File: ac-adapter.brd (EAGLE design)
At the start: 98.4 x 49.5 mm, 55 parts, among them IC1 STR-Y6735, IC2 TL431, Q1 TLP621-1, T1 COMMON_FILTER-SU10VFC, T2 TRANSFORMAER_FLYBACK-PQ2620

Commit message: 微修正
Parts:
- added HT1: HEATSINK-2, my_connector:HEATSINK2
- D5, D6: value 0.1A -> 1N4148; device my_rcl:D0207/2V -> my_rcl:SOD123
- R3: device my_rcl:0207/2V -> my_rcl:1608
- R7, R8: device my_rcl:0207/2V -> my_rcl:2012
- moved C5 2.69 mm to (14.6, 8.26)
- moved IC1 2.29 mm to (26.7, 8.26)
- moved D5 2.25 mm to (23.5, 18.1), flipped to the bottom
- moved D6 2.06 mm to (26.7, 16.7), flipped to the bottom, turned to 0 degrees
- moved C3 1.91 mm to (35.6, 16.5)
- moved R3 1.91 mm to (26.7, 19.1), flipped to the bottom, turned to 180 degrees
- moved R4 1.91 mm to (21.3, 18.1)
- moved C4 1.90 mm to (35.6, 13.0)
- moved C6 1.90 mm to (21.3, 14.3)
- moved C7 1.90 mm to (24.1, 6.35)
- moved R5 1.90 mm to (19.4, 14.3)
- moved R1 1.90 mm to (30.2, 21.9)
- moved C17 1.27 mm to (29.8, 23.2)
- moved SJ1 0.79 mm to (84.0, 6.67)
- moved R7 0.71 mm to (80.6, 11.7), flipped to the bottom
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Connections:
- net PGND: now also HT1.HT1
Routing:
- net PGND: track 138.9 -> 151.5 mm
- net VCC: track 22.0 -> 28.7 mm
- net SW: track 33.3 -> 31.4 mm
- net N$15: track 38.3 -> 36.7 mm
- net N$6: track 29.2 -> 30.6 mm
- net N$11: track 13.3 -> 12.2 mm
- net V+: track 31.5 -> 32.4 mm
- net N$23: track 27.4 -> 26.7 mm
- net VP: track 26.5 -> 25.9 mm
- net N$10: track 4.49 -> 5.13 mm
- removed copper zone on layer 1, net PGND
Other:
- board text added: "QR AC adapter"
- board text removed: "QR AC adapter ±20V2A"

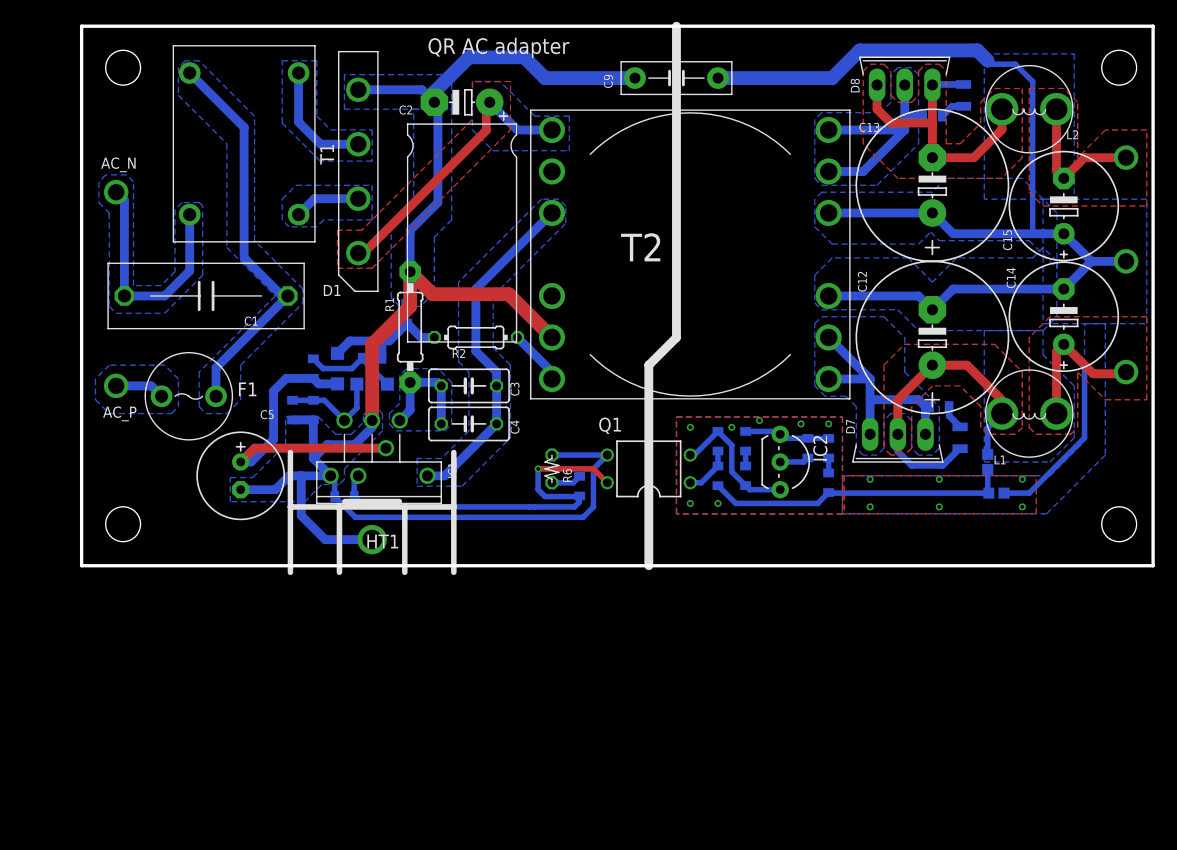
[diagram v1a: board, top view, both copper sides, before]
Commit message: BM1Q011FJを使う
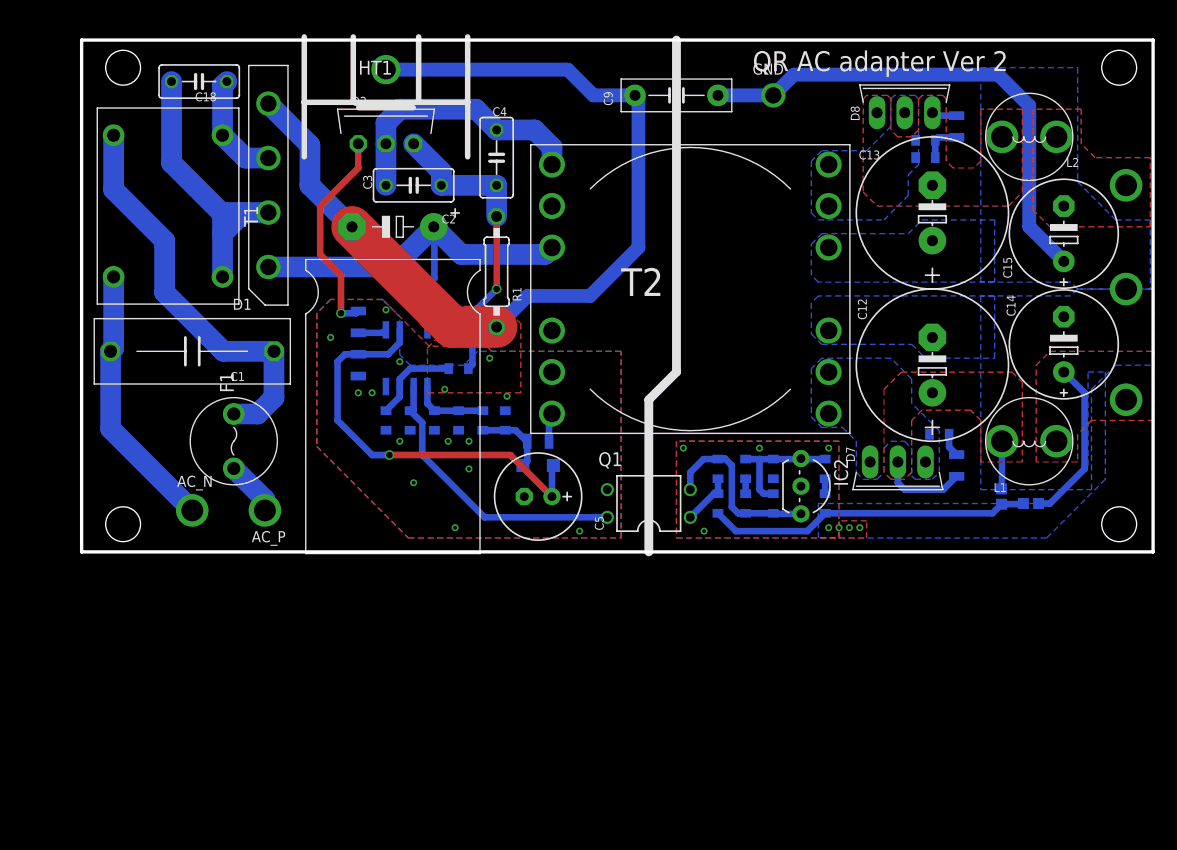
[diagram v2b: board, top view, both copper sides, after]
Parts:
- removed D6: 1N4148, my_rcl:SOD123
- added C18: 1000pX, my_rcl:C050
- added C19: DNP, my_rcl:1608
- added C20: 1n, my_rcl:1608
- added Q2: 600V5A, my_ic:TO-220
- added R15: 10k, my_rcl:2012
- added R16: 1k, my_rcl:1608
- added TP6: GND, my_connector:TESTPIN-BIG
- C2: device my_rcl:E5-10,5A2 -> my_rcl:E5-16A2
- C7: value 1000p -> 100p
- C8: value 0.22u -> 0.1u; device my_rcl:1608 -> my_rcl:2012
- D1: value 1000V1A -> 600V1A
- F1: value 1A250V -> 1A125V
- IC1: value STR-Y6735 -> BM1Q011; device my_ic:TO220F-7L-3051 -> my_ic:SOP8-J7S
- R2: device my_rcl:0204/7 -> my_rcl:2012
- R3: value 6.8k -> 10; device my_rcl:1608 -> my_rcl:2012
- R4: value DNP -> 10k
- R6: value 100k -> 10k; device my_rcl:0207/2V -> my_rcl:1608
- T2: value TRANSFORMAER_FLYBACK-PQ2620 -> TRANSFORMAER_FLYBACK-PQ2620-2
- TP1, TP2, TP3, TP4, TP5: device my_connector:TESTPIN-BIG -> my_connector:TESTPIN-LARGE
- moved R6 44.6 mm to (77.5, 37.5), flipped to the bottom, turned to 0 degrees
- moved HT1 37.2 mm to (27.9, 42.5), turned to 0 degrees
- moved TP2 30.0 mm to (10.2, 5.08)
- moved C5 27.4 mm to (41.9, 6.35), turned to 180 degrees
- moved C4 24.6 mm to (38.1, 37.5), turned to 270 degrees
- moved C8 23.2 mm to (25.4, 18.4)
- moved D5 20.4 mm to (41.9, 9.21), turned to 180 degrees
- moved C3 19.1 mm to (30.5, 34.9), turned to 0 degrees
- moved TP1 17.8 mm to (16.8, 5.08)
- moved R4 16.3 mm to (36.8, 13.3)
- moved R5 15.3 mm to (34.6, 13.3), turned to 90 degrees
- moved C17 13.4 mm to (38.9, 13.3)
- moved C2 13.1 mm to (28.6, 31.1), turned to 0 degrees
- moved IC1 11.3 mm to (29.8, 19.1), flipped to the bottom, turned to 0 degrees
- moved C6 11.2 mm to (32.4, 13.3)
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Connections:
- new net N$12: C3.2, C4.2, Q2.3, R1.2, R16.1
- new net N$19: C7.1, IC1.2, Q1.4
- net GND: now also TP6.1
- net N$11: now also R4.2; no longer R3.2
- net N$13: now also IC1.5, R3.2; no longer C6.1, D6.2, IC1.6, R5.1
- net N$14: now also Q2.1; no longer D6.1, R4.1
- net N$15: now also C19.1, IC1.3, R16.2; no longer C7.2, C8.2, IC1.5, Q1.4
- net N$16: now also C18.1, D1.3, T1.3; no longer C8.1, R6.2
- net N$18: now also R6.2
- net N$22: now also R6.1
- net N$26: now also C20.1
- net N$28: now also C20.2
- net N$4: now also C18.2
- net N$5: now also IC1.8, R15.1; no longer D1.3, T1.3
- net N$7: now also C6.1, IC1.1, R4.1, R5.2; no longer C3.2, C4.2, IC1.2, R1.2
- net PGND: now also C19.2, C7.2, C8.2, R5.1; no longer C7.1, IC1.7, R5.2, R6.1
- net SW: now also Q2.2, T2.1; no longer IC1.1, T2.3
- net VCC: now also C8.1, IC1.6; no longer IC1.3, R4.2
- net VP: now also R15.2, T2.3; no longer T2.1
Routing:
- net PGND: track 151.5 -> 85.6 mm, vias 0 -> 15
- net GND: track 103.4 -> 46.2 mm, vias 13 -> 8
- net N$15: track 36.7 -> 8.33 mm, vias 1 -> 0
- net N$12: track 0.00 -> 27.8 mm, vias 0 -> 1
- net N$19: track 0.00 -> 26.4 mm
- net N$23: track 26.7 -> 2.33 mm
- net N$17: track 22.5 -> 0.00 mm
- net N$18: track 21.3 -> 0.00 mm
- net N$4: track 6.08 -> 26.8 mm
- net N$6: track 30.6 -> 12.5 mm
- net V+: track 32.4 -> 15.2 mm
- net V-: track 13.1 -> 0.00 mm
- net N$14: track 8.60 -> 19.5 mm, vias 0 -> 1
- net VCC: track 28.7 -> 38.5 mm, vias 0 -> 1
- net VP: track 25.9 -> 34.4 mm
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- added copper zone on layer 1, net PGND
- removed copper zone on layer 16, net N$1
- removed copper zone on layer 16, net N$2
- removed copper zone on layer 16, net N$3
- removed copper zone on layer 16, net N$4
- removed copper zone on layer 16, net N$5
- removed copper zone on layer 16, net N$7
- removed copper zone on layer 16, net SW
- removed copper zone on layer 1, net VP
- removed copper zone on layer 16, net VP
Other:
- board size 98.4 x 49.5 mm -> 98.4 x 47 mm
- board text added: "QR AC adapter Ver 2"
- board text removed: "QR AC adapter"

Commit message: PGND変更
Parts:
- added FB1: FB, my_rcl:1608-J
- moved HT1 1.91 mm to (27.9, 40.6)
- moved R16 1.42 mm to (35.2, 16.8)
- moved C11 1.27 mm to (77.5, 37.8)
- moved C18 1.27 mm to (10.8, 43.2)
- moved C4 1.27 mm to (38.1, 36.2)
- moved C9 1.27 mm to (54.6, 41.9)
- moved D8 1.27 mm to (75.6, 40.3)
- moved R6 1.27 mm to (77.5, 36.2)
- moved T1 1.27 mm to (7.94, 31.8)
- moved TP6 1.27 mm to (63.5, 41.9)
- moved C17 1.27 mm to (38.9, 12.1)
- moved C19 1.27 mm to (27.9, 12.1)
- moved C6 1.27 mm to (32.4, 12.1)
- moved C7 1.27 mm to (30.2, 12.1)
- moved R4 1.27 mm to (36.8, 12.1)
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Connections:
- new net N$20: FB1.1, HT1.HT1
- net PGND: now also FB1.2; no longer HT1.HT1
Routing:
- net PGND: track 85.6 -> 80.5 mm, vias 15 -> 19
- net N$20: track 0.00 -> 4.03 mm
- net VCC: track 38.5 -> 35.6 mm
- net N$11: track 6.88 -> 7.88 mm
- net N$1: track 5.03 -> 5.78 mm
- net N$15: track 8.33 -> 8.96 mm

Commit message: tiny
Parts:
- added D2: GREEN, my_rcl:D1608
- added R17, R18: 10k, my_rcl:1608
- added V1: Varistor, my_rcl:C050
- moved F1 1.59 mm to (15.6, 10.2)
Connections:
- new net N$21: D2.K, R17.2
- net GND: now also R17.1
- net N$14: now also R18.1
- net N$2: now also V1.2
- net N$3: now also V1.1
- net N$9: now also D2.A
- net PGND: now also R18.2
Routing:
- net N$3: track 37.2 -> 42.6 mm
- net N$9: track 29.8 -> 34.0 mm, vias 0 -> 1
- net N$21: track 0.00 -> 2.54 mm
- net N$1: track 5.78 -> 4.38 mm
- net N$14: track 19.5 -> 20.8 mm
- net GND: vias 8 -> 7

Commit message: GaN
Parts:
- removed FB1: FB, my_rcl:1608-J
- removed HT1: HEATSINK-2, my_connector:HEATSINK2
- removed Q2: 600V5A, my_ic:TO-220
- removed R18: 10k, my_rcl:1608
- added C21: (no value), my_rcl:1608
- added D3: (no value), my_rcl:SOD123
- added IC3: NV6113, my_ic:NV6113
- R3: value 10 -> (none); device my_rcl:2012 -> my_rcl:1608
- moved R3 48.7 mm to (-3.49, -18.1), flipped to the top, turned to 0 degrees
- moved C3 4.85 mm to (34.6, 36.2), turned to 270 degrees
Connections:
- new net N$24: D3.2, IC3.4
- net N$12: now also C21.2, D3.1, IC3.S; no longer Q2.3
- net N$13: now also IC3.2; no longer R3.2
- net N$14: now also C21.1; no longer Q2.1, R18.1
- net N$20: now also IC3.3, R3.2; no longer FB1.1, HT1.HT1
- net PGND: no longer FB1.2, R18.2
- net SW: now also IC3.D, IC3.D1, IC3.D2, IC3.D3, IC3.D4; no longer Q2.2
- net VCC: now also IC3.1
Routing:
- net N$14: track 20.8 -> 0.00 mm, vias 1 -> 0
- net SW: track 24.1 -> 3.83 mm
- net N$12: track 27.6 -> 14.8 mm
- net N$20: track 4.03 -> 0.00 mm
- net N$13: track 2.65 -> 0.38 mm
- net PGND: track 80.5 -> 79.3 mm
